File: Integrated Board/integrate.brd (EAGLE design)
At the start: 150 x 120 mm, 67 parts, among them U1 LM293D-SOIC8, U2 LM293D-SOIC8, U3 LM293D-SOIC8, U4 LM293D-SOIC8, U5 LM293D-SOIC8, U6 LM293D-SOIC8, U7 LM293D-SOIC8, U8 LM293D-SOIC8

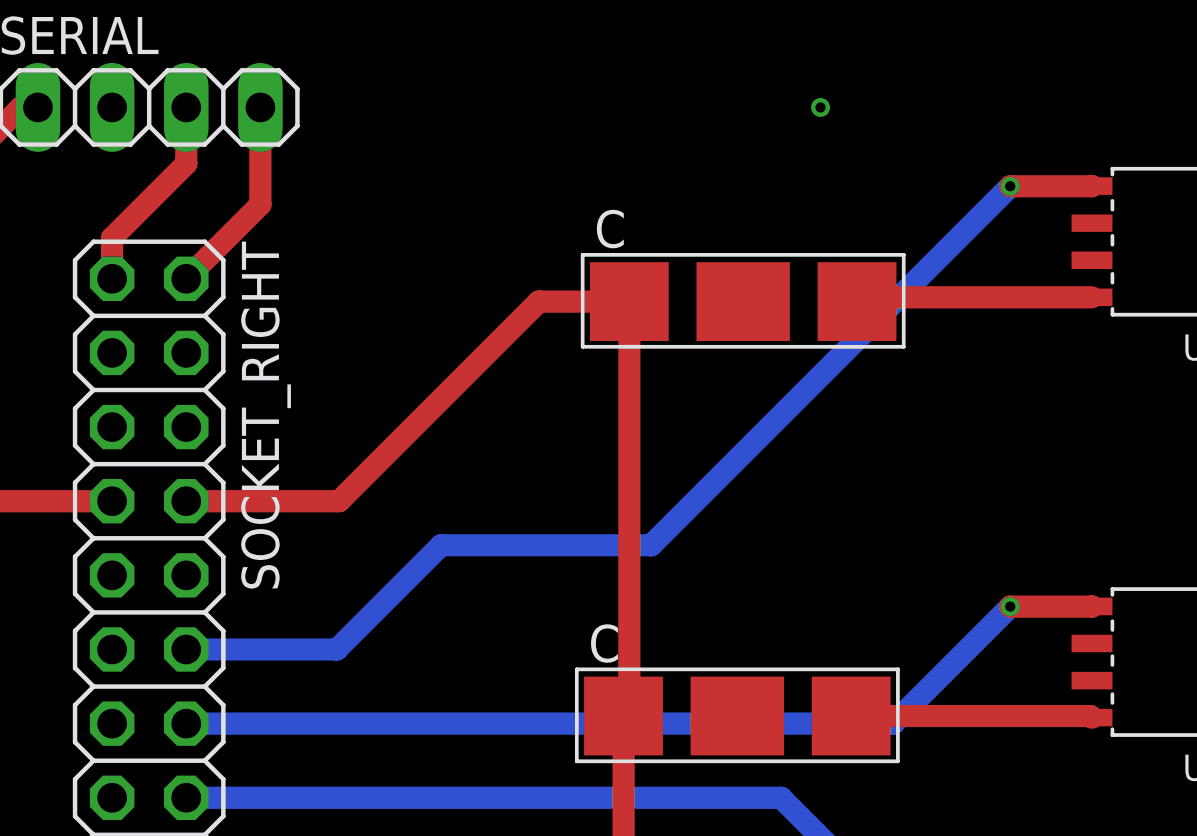
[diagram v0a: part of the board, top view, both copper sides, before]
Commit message: 20180719-Fix-problem-for-LVB
1. OSC part: left top 6th channel cannot be arranged, change pin to left top 5th

2.change the area of HVB
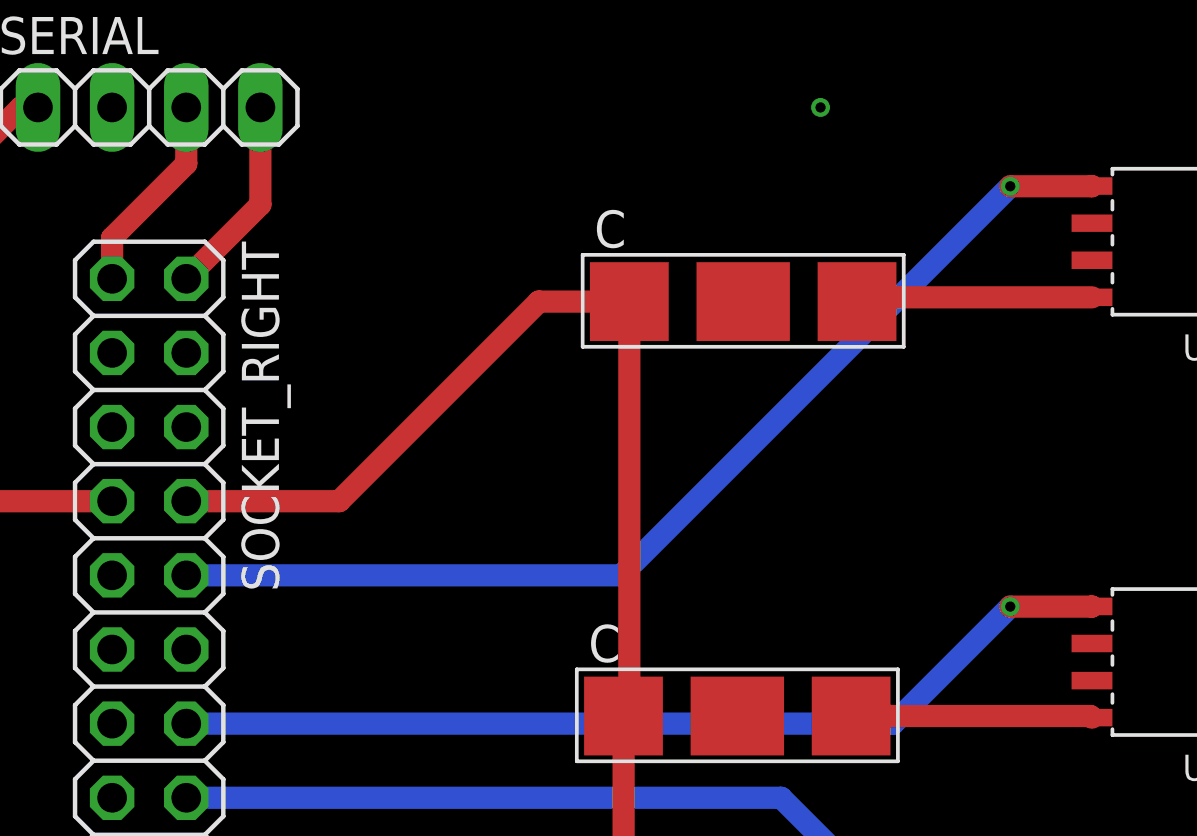
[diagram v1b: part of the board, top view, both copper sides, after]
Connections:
- net S1: now also SOCKET_RIGHT.10; no longer SOCKET_RIGHT.12
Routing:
- net S1: track 37.6 -> 36.6 mm
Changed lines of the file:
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@@
 <signal name="S1">
 <contactref element="U1" pad="5"/>
-<contactref element="SOCKET_RIGHT" pad="12"/>
 <via x="169.5" y="112.3" extent="1-16" drill="0.35"/>
 <wire x1="169.5" y1="112.3" x2="172.295" y2="112.3" width="0.762" layer="1"/>
 <wire x1="172.295" y1="112.3" x2="172.3" y2="112.305" width="0.762" layer="1"/>
-<wire x1="169.5" y1="112.3" x2="157.2" y2="100" width="0.762" layer="16"/>
-<wire x1="157.2" y1="100" x2="150" y2="100" width="0.762" layer="16"/>
-<wire x1="150" y1="100" x2="146.43" y2="96.43" width="0.762" layer="16"/>
-<wire x1="146.43" y1="96.43" x2="141.27" y2="96.43" width="0.762" layer="16"/>
+<contactref element="SOCKET_RIGHT" pad="10"/>
+<wire x1="156.17" y1="98.97" x2="141.27" y2="98.97" width="0.762" layer="16"/>
+<wire x1="169.5" y1="112.3" x2="156.17" y2="98.97" width="0.762" layer="16"/>
 </signal>
 <signal name="S2">

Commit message: Revert "20180712-change-pin"
This reverts commit fb38f18733497d936434fddb3c409504ab7d6048.
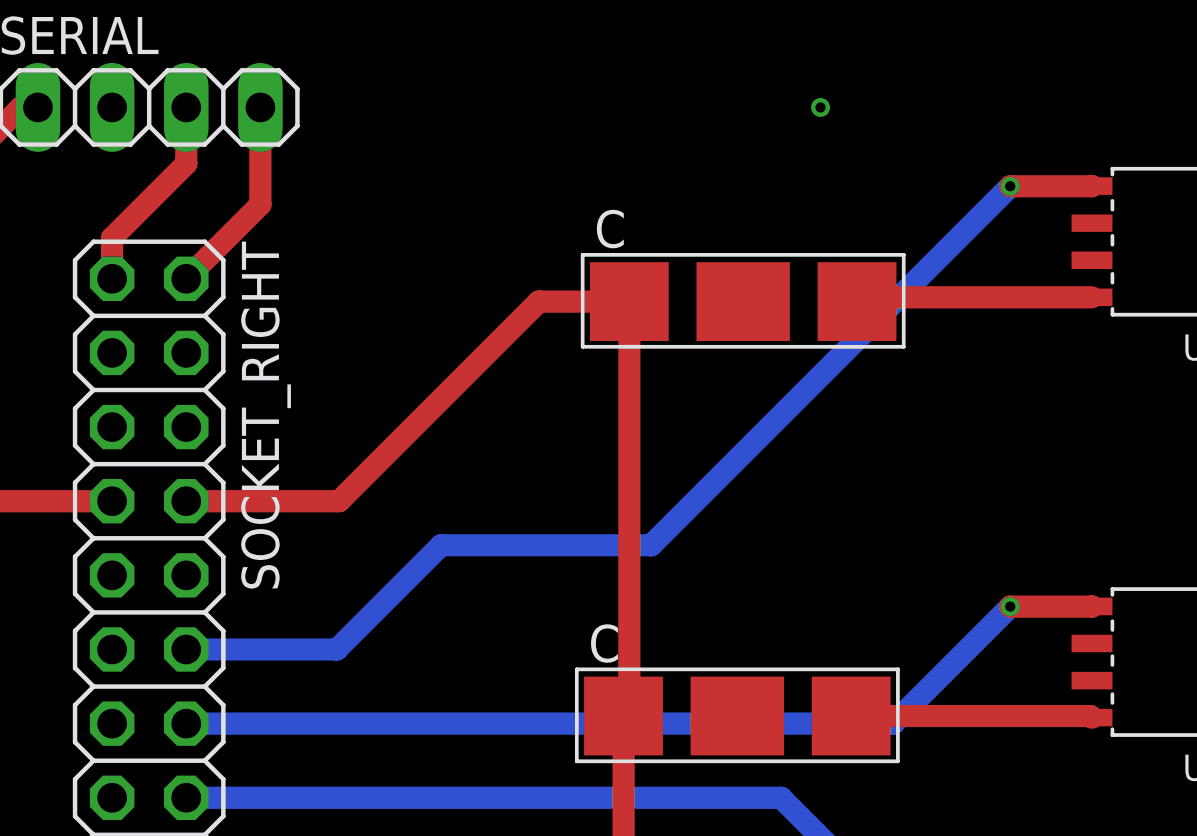
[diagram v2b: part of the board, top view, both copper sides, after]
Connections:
- net S1: now also SOCKET_RIGHT.12; no longer SOCKET_RIGHT.10
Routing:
- net S1: track 36.6 -> 37.6 mm
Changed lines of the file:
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@@
 <signal name="S1">
 <contactref element="U1" pad="5"/>
+<contactref element="SOCKET_RIGHT" pad="12"/>
 <via x="169.5" y="112.3" extent="1-16" drill="0.35"/>
 <wire x1="169.5" y1="112.3" x2="172.295" y2="112.3" width="0.762" layer="1"/>
 <wire x1="172.295" y1="112.3" x2="172.3" y2="112.305" width="0.762" layer="1"/>
-<contactref element="SOCKET_RIGHT" pad="10"/>
-<wire x1="156.17" y1="98.97" x2="141.27" y2="98.97" width="0.762" layer="16"/>
-<wire x1="169.5" y1="112.3" x2="156.17" y2="98.97" width="0.762" layer="16"/>
+<wire x1="169.5" y1="112.3" x2="157.2" y2="100" width="0.762" layer="16"/>
+<wire x1="157.2" y1="100" x2="150" y2="100" width="0.762" layer="16"/>
+<wire x1="150" y1="100" x2="146.43" y2="96.43" width="0.762" layer="16"/>
+<wire x1="146.43" y1="96.43" x2="141.27" y2="96.43" width="0.762" layer="16"/>
 </signal>
 <signal name="S2">
